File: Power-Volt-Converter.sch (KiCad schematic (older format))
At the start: 28 parts, among them P22 XT60, P23 XT60, P24 XT60, P25 XT60, P26 XT60, P27 XT60, P28 XT60, P29 XT60, Q9 BC817-40, U10 I6A24014A033V, U7 UWE-12/6-Q12P, U8 TEN_20-2411WIN, U9 TEN_20-2411WIN

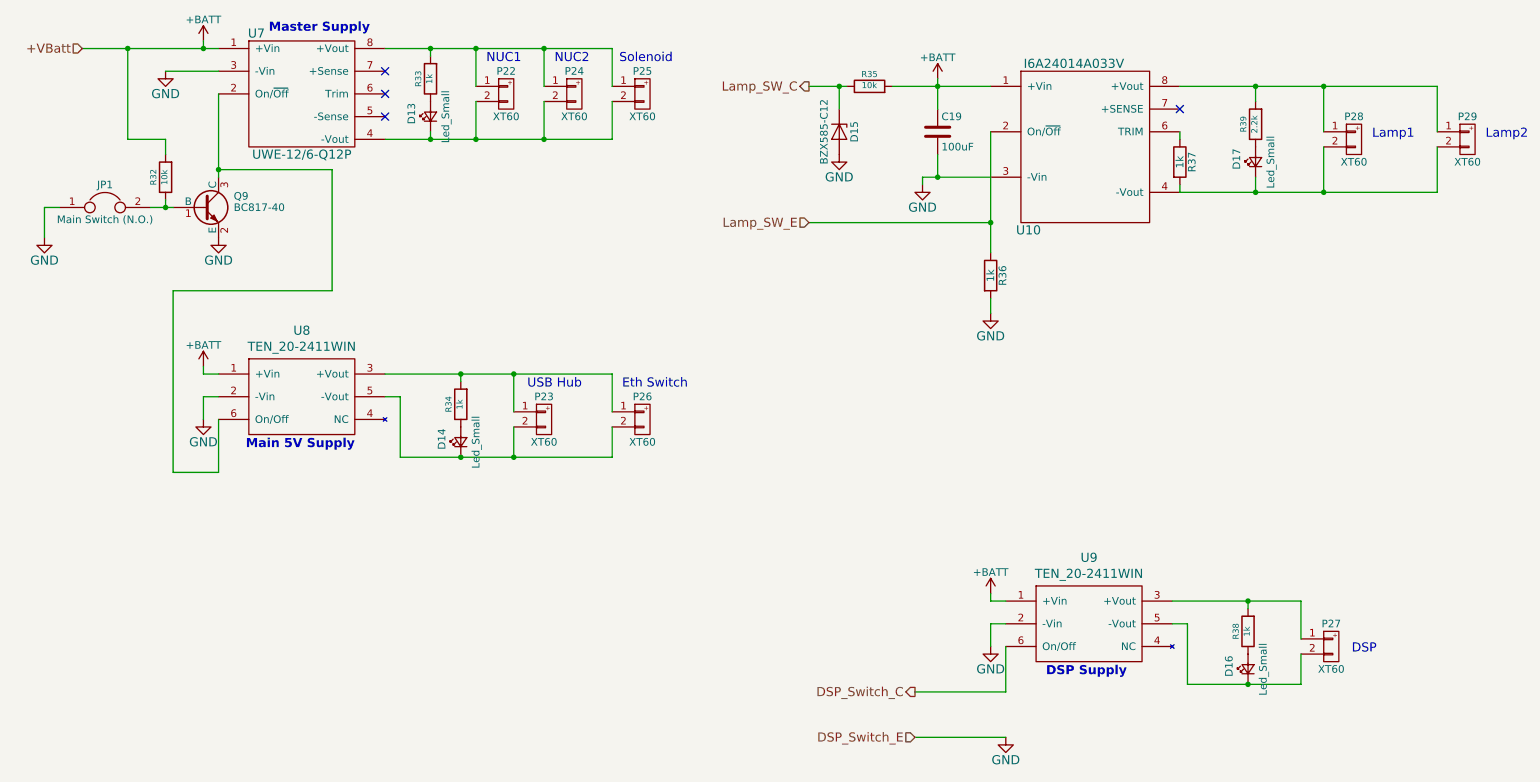
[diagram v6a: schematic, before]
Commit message: change circuit for i6a negative logic on/off
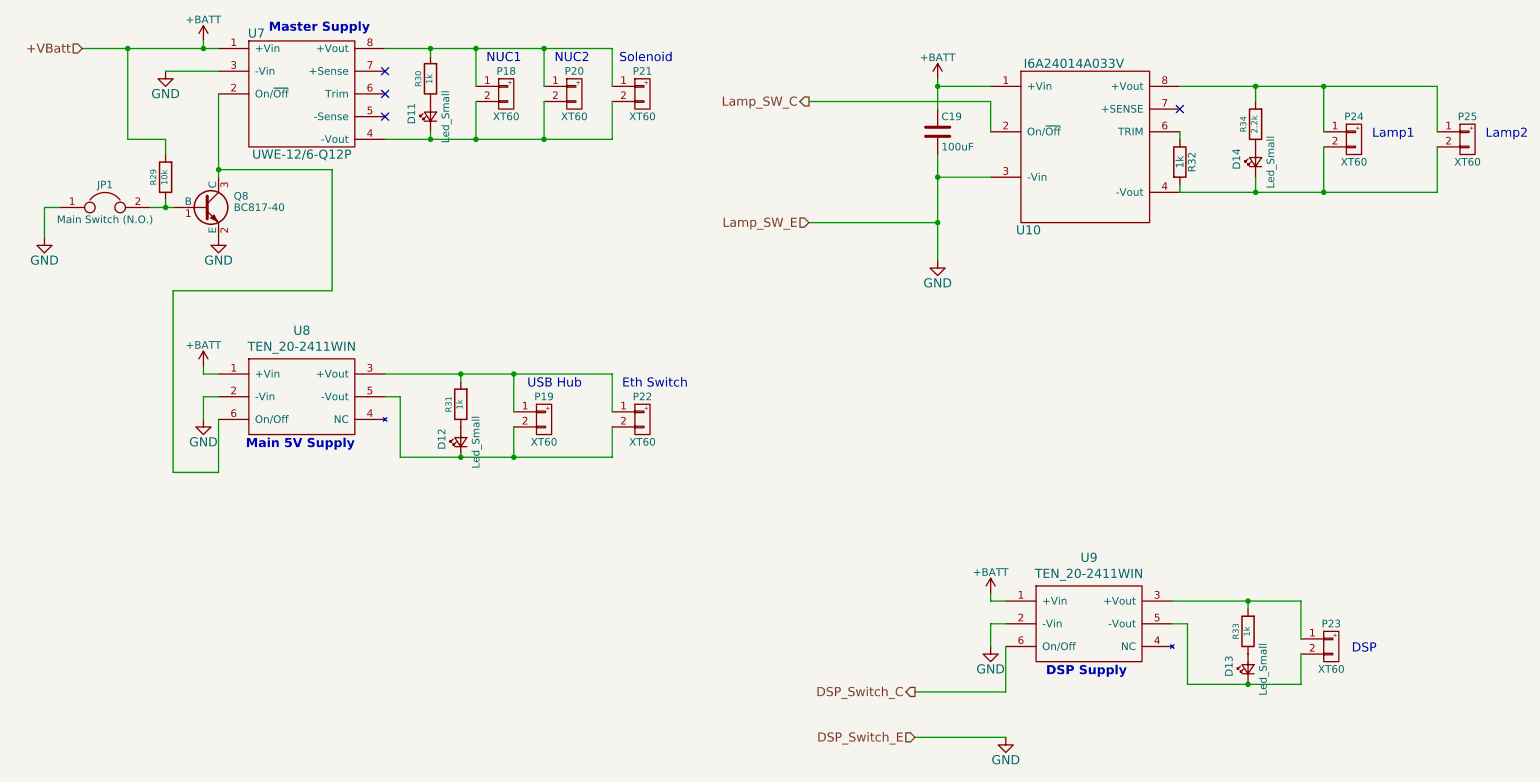
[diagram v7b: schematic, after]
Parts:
- removed D15: BZX585-C12, Diodes_SMD:D_SOD-523, symbol D_Zener
- removed R35: 10k, Resistors_SMD:R_0603, symbol R
- removed R36: 1k, Resistors_SMD:R_0603, symbol R
- renumbered D13 to D11, D14 to D12, D16 to D13, D17 to D14, P22 to P18, P23 to P19, P24 to P20, P25 to P21, P26 to P22, P27 to P23, P28 to P24, P29 to P25, Q9 to Q8, R32 to R29, R33 to R30, R34 to R31, R37 to R32, R38 to R33, R39 to R34
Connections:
- net Lamp_SW_E is gone; now on net Lamp_SW_C: U10.2 (On/~Off)
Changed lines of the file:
@@
 LIBS:zeabus
 LIBS:ftdi
+LIBS:Power_Distributor-cache
 EELAYER 25 0
 EELAYER END
@@
 L GND #PWR044
 U 1 1 58C84F3D
-P 7250 2350
-F 0 "#PWR044" H 7250 2100 60  0001 C CNN
-F 1 "GND" H 7250 2200 60  0000 C CNN
-F 2 "" H 7250 2350 60  0000 C CNN
-F 3 "" H 7250 2350 60  0000 C CNN
-	1    7250 2350
+P 7350 2850
+F 0 "#PWR044" H 7350 2600 60  0001 C CNN
+F 1 "GND" H 7350 2700 60  0000 C CNN
+F 2 "" H 7350 2850 60  0000 C CNN
+F 3 "" H 7350 2850 60  0000 C CNN
+	1    7350 2850
 	1    0    0    -1
 $EndComp
@@
 $EndComp
 $Comp
-L R R33
+L R R30
 U 1 1 58C85083
 P 4000 1650
-F 0 "R33" V 4080 1650 40  0000 C CNN
+F 0 "R30" V 4080 1650 40  0000 C CNN
 F 1 "1k" V 4007 1651 40  0000 C CNN
 F 2 "Resistors_SMD:R_0603" V 3930 1650 30  0001 C CNN
@@
 $EndComp
 $Comp
-L LED_Small D13
+L LED_Small D11
 U 1 1 58C85089
 P 4000 1900
-F 0 "D13" H 3950 2025 50  0000 L CNN
+F 0 "D11" H 3950 2025 50  0000 L CNN
 F 1 "Led_Small" H 3825 1800 50  0000 L CNN
 F 2 "LEDs:LED_0603" V 4000 1900 60  0001 C CNN
@@
 $EndComp
 $Comp
-L XT60 P22
+L XT60 P18
 U 1 1 58C8508F
 P 4500 1750
-F 0 "P22" H 4500 1900 50  0000 C CNN
+F 0 "P18" H 4500 1900 50  0000 C CNN
 F 1 "XT60" H 4500 1600 50  0000 C CNN
 F 2 "Zeabus:XT60" H 4500 1750 60  0001 C CNN
@@
 $EndComp
 $Comp
-L R R34
+L R R31
 U 1 1 58C85236
 P 4200 3800
-F 0 "R34" V 4280 3800 40  0000 C CNN
+F 0 "R31" V 4280 3800 40  0000 C CNN
 F 1 "1k" V 4207 3801 40  0000 C CNN
 F 2 "Resistors_SMD:R_0603" V 4130 3800 30  0001 C CNN
@@
 $EndComp
 $Comp
-L LED_Small D14
+L LED_Small D12
 U 1 1 58C8523C
 P 4200 4050
-F 0 "D14" H 4150 4175 50  0000 L CNN
+F 0 "D12" H 4150 4175 50  0000 L CNN
 F 1 "Led_Small" H 4025 3950 50  0000 L CNN
 F 2 "LEDs:LED_0603" V 4200 4050 60  0001 C CNN
@@
 $EndComp
 $Comp
-L XT60 P23
+L XT60 P19
 U 1 1 58C85242
 P 4750 3900
-F 0 "P23" H 4750 4050 50  0000 C CNN
+F 0 "P19" H 4750 4050 50  0000 C CNN
 F 1 "XT60" H 4750 3750 50  0000 C CNN
 F 2 "Zeabus:XT60" H 4750 3900 60  0001 C CNN
@@
 $EndComp
 $Comp
-L BC817-40 Q9
+L BC817-40 Q8
 U 1 1 58C81AD3
 P 2500 2500
-F 0 "Q9" H 2700 2575 50  0000 L CNN
+F 0 "Q8" H 2700 2575 50  0000 L CNN
 F 1 "BC817-40" H 2700 2500 50  0000 L CNN
 F 2 "TO_SOT_Packages_SMD:SOT-23" H 2700 2425 50  0001 L CIN
@@
 $EndComp
 $Comp
-L R R32
+L R R29
 U 1 1 58C8A817
 P 2250 2300
-F 0 "R32" V 2330 2300 40  0000 C CNN
+F 0 "R29" V 2330 2300 40  0000 C CNN
 F 1 "10k" V 2257 2301 40  0000 C CNN
 F 2 "Resistors_SMD:R_0603" V 2180 2300 30  0001 C CNN
@@
 $EndComp
 $Comp
-L XT60 P24
+L XT60 P20
 U 1 1 58C8B481
 P 4950 1750
-F 0 "P24" H 4950 1900 50  0000 C CNN
+F 0 "P20" H 4950 1900 50  0000 C CNN
 F 1 "XT60" H 4950 1600 50  0000 C CNN
 F 2 "Zeabus:XT60" H 4950 1750 60  0001 C CNN
@@
 Master Supply
 $Comp
-L XT60 P25
+L XT60 P21
 U 1 1 58C8BA0B
 P 5400 1750
-F 0 "P25" H 5400 1900 50  0000 C CNN
+F 0 "P21" H 5400 1900 50  0000 C CNN
 F 1 "XT60" H 5400 1600 50  0000 C CNN
 F 2 "Zeabus:XT60" H 5400 1750 60  0001 C CNN
@@
 Lamp1
 $Comp
-L XT60 P29
+L XT60 P25
 U 1 1 58C8E09C
 P 10850 2050
-F 0 "P29" H 10850 2200 50  0000 C CNN
+F 0 "P25" H 10850 2200 50  0000 C CNN
 F 1 "XT60" H 10850 1900 50  0000 C CNN
 F 2 "Zeabus:XT60" H 10850 2050 60  0001 C CNN
@@
 	1    0    0    -1
 $EndComp
-Text HLabel 6500 1700 0    60   Output ~ 0
+Text HLabel 6500 1800 0    60   Output ~ 0
 Lamp_SW_C
 Text HLabel 6500 2600 0    60   Input ~ 0
@@
 Eth Switch
 $Comp
-L R R38
+L R R33
 U 1 1 58C90964
 P 9400 5300
-F 0 "R38" V 9480 5300 40  0000 C CNN
+F 0 "R33" V 9480 5300 40  0000 C CNN
 F 1 "1k" V 9407 5301 40  0000 C CNN
 F 2 "Resistors_SMD:R_0603" V 9330 5300 30  0001 C CNN
@@
 $EndComp
 $Comp
-L LED_Small D16
+L LED_Small D13
 U 1 1 58C9096A
 P 9400 5550
-F 0 "D16" H 9350 5675 50  0000 L CNN
+F 0 "D13" H 9350 5675 50  0000 L CNN
 F 1 "Led_Small" H 9225 5450 50  0000 L CNN
 F 2 "LEDs:LED_0603" V 9400 5550 60  0001 C CNN
@@
 $EndComp
 $Comp
-L XT60 P27
+L XT60 P23
 U 1 1 58C90970
 P 9950 5400
-F 0 "P27" H 9950 5550 50  0000 C CNN
+F 0 "P23" H 9950 5550 50  0000 C CNN
 F 1 "XT60" H 9950 5250 50  0000 C CNN
 F 2 "Zeabus:XT60" H 9950 5400 60  0001 C CNN
@@
 USB Hub
 $Comp
-L XT60 P26
+L XT60 P22
 U 1 1 58C90D7F
 P 5400 3900
-F 0 "P26" H 5400 4050 50  0000 C CNN
+F 0 "P22" H 5400 4050 50  0000 C CNN
 F 1 "XT60" H 5400 3750 50  0000 C CNN
 F 2 "Zeabus:XT60" H 5400 3900 60  0001 C CNN
@@
 Text HLabel 7200 6000 0    60   Input ~ 0
 DSP_Switch_E
-$Comp
-L D_Zener D15
-U 1 1 58E6F6E6
-P 6700 2000
-F 0 "D15" H 6700 2100 50  0000 C CNN
-F 1 "BZX585-C12" H 6700 1900 50  0000 C CNN
-F 2 "Diodes_SMD:D_SOD-523" H 6700 2000 50  0001 C CNN
-F 3 "" H 6700 2000 50  0001 C CNN
-	1    6700 2000
-	0    1    1    0
-$EndComp
-$Comp
-L R R35
-U 1 1 58E6F94F
-P 6900 1700
-F 0 "R35" V 6980 1700 40  0000 C CNN
-F 1 "10k" V 6907 1701 40  0000 C CNN
-F 2 "Resistors_SMD:R_0603" V 6830 1700 30  0001 C CNN
-F 3 "" H 6900 1700 30  0000 C CNN
-	1    6900 1700
-	0    -1   -1   0
-$EndComp
-$Comp
-L GND #PWR055
-U 1 1 58E6FD35
-P 6700 2150
-F 0 "#PWR055" H 6700 1900 60  0001 C CNN
-F 1 "GND" H 6700 2000 60  0000 C CNN
-F 2 "" H 6700 2150 60  0000 C CNN
-F 3 "" H 6700 2150 60  0000 C CNN
-	1    6700 2150
-	1    0    0    -1
-$EndComp
 $Comp
 L I6A24014A033V U10
@@
 $EndComp
 $Comp
-L XT60 P28
+L XT60 P24
 U 1 1 58C84F61
 P 10100 2050
-F 0 "P28" H 10100 2200 50  0000 C CNN
+F 0 "P24" H 10100 2200 50  0000 C CNN
 F 1 "XT60" H 10100 1900 50  0000 C CNN
 F 2 "Zeabus:XT60" H 10100 2050 60  0001 C CNN
@@
 $EndComp
 $Comp
-L R R37
+L R R32
 U 1 1 58EFA965
 P 8950 2200
-F 0 "R37" V 9030 2200 50  0000 C CNN
+F 0 "R32" V 9030 2200 50  0000 C CNN
 F 1 "1k" V 8950 2200 50  0000 C CNN
 F 2 "Resistors_SMD:R_0603" V 8880 2200 50  0001 C CNN
@@
 $EndComp
 Wire Wire Line
-	7050 1700 7700 1700
-Wire Wire Line
 	2250 1600 2600 1600
 Wire Wire Line
@@
 Connection ~ 2600 2250
 Wire Wire Line
-	6500 1700 6750 1700
-Connection ~ 7350 1700
-Wire Wire Line
-	6700 1700 6700 1850
-Connection ~ 6700 1700
-Wire Wire Line
 	8950 2400 10650 2400
 Wire Wire Line
@@
 	8950 2350 8950 2400
 Wire Wire Line
-	7250 2350 7250 2300
-Wire Wire Line
-	7250 2300 7700 2300
-Wire Wire Line
-	7350 2150 7350 2300
-Connection ~ 7350 2300
-$Comp
-L R R39
+	7350 2150 7350 2850
+$Comp
+L R R34
 U 1 1 58F01219
 P 9450 1950
-F 0 "R39" V 9530 1950 40  0000 C CNN
+F 0 "R34" V 9530 1950 40  0000 C CNN
 F 1 "2.2k" V 9457 1951 40  0000 C CNN
 F 2 "Resistors_SMD:R_0603" V 9380 1950 30  0001 C CNN
@@
 $EndComp
 $Comp
-L LED_Small D17
+L LED_Small D14
 U 1 1 58F0121F
 P 9450 2200
-F 0 "D17" H 9400 2325 50  0000 L CNN
+F 0 "D14" H 9400 2325 50  0000 L CNN
 F 1 "Led_Small" H 9275 2100 50  0000 L CNN
 F 2 "LEDs:LED_0603" V 9450 2200 60  0001 C CNN
@@
 Connection ~ 9450 2400
 Wire Wire Line
-	6500 2600 7700 2600
-Wire Wire Line
-	7700 2000 7700 2800
-Wire Wire Line
 	7350 1650 7350 1850
-$Comp
-L R R36
-U 1 1 58F08F01
-P 7700 2950
-F 0 "R36" V 7780 2950 50  0000 C CNN
-F 1 "1k" V 7700 2950 50  0000 C CNN
-F 2 "Resistors_SMD:R_0603" V 7630 2950 50  0001 C CNN
-F 3 "" H 7700 2950 50  0001 C CNN
-	1    7700 2950
-	1    0    0    -1
-$EndComp
-Connection ~ 7700 2600
-Wire Wire Line
-	7700 3100 7700 3200
-$Comp
-L GND #PWR056
-U 1 1 58F09347
-P 7700 3200
-F 0 "#PWR056" H 7700 2950 60  0001 C CNN
-F 1 "GND" H 7700 3050 60  0000 C CNN
-F 2 "" H 7700 3200 60  0000 C CNN
-F 3 "" H 7700 3200 60  0000 C CNN
-	1    7700 3200
-	1    0    0    -1
-$EndComp
 NoConn ~ 3700 1600
 NoConn ~ 3700 1750
 NoConn ~ 3700 1900
 NoConn ~ 8950 1850
+Wire Wire Line
+	7700 1700 7350 1700
+Connection ~ 7350 1700
+Wire Wire Line
+	6500 1800 7700 1800
+Wire Wire Line
+	7700 1800 7700 2000
+Wire Wire Line
+	7350 2600 6500 2600
+Connection ~ 7350 2600
+Wire Wire Line
+	7700 2300 7350 2300
+Connection ~ 7350 2300
 $EndSCHEMATC

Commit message: change footprint of Main Switch from 2.00mm to 2.54mm
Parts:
- JP1: footprint Pin_Headers:Pin_Header_Straight_1x02_Pitch2.00mm -> Pin_Headers:Pin_Header_Straight_1x02_Pitch2.54mm
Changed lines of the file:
@@
 LIBS:zeabus
 LIBS:ftdi
-LIBS:Power_Distributor-cache
 EELAYER 25 0
 EELAYER END
@@
 F 0 "JP1" H 1850 2650 50  0000 C CNN
 F 1 "Main Switch (N.O.)" H 1850 2420 50  0000 C CNN
-F 2 "Pin_Headers:Pin_Header_Straight_1x02_Pitch2.00mm" H 1850 2500 60  0001 C CNN
+F 2 "Pin_Headers:Pin_Header_Straight_1x02_Pitch2.54mm" H 1850 2500 60  0001 C CNN
 F 3 "" H 1850 2500 60  0000 C CNN
 	1    1850 2500
